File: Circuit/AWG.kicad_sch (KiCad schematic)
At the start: 28 parts, among them J1 Power, J2 Pump 1, J3 Pump 2, J4 Pump 3, M1 Fan_3pin, M2 Fan_3pin, Q1 RFP30N06LE, Q2 RFP30N06LE, SW1 Switch, U2 LCD-016N002L

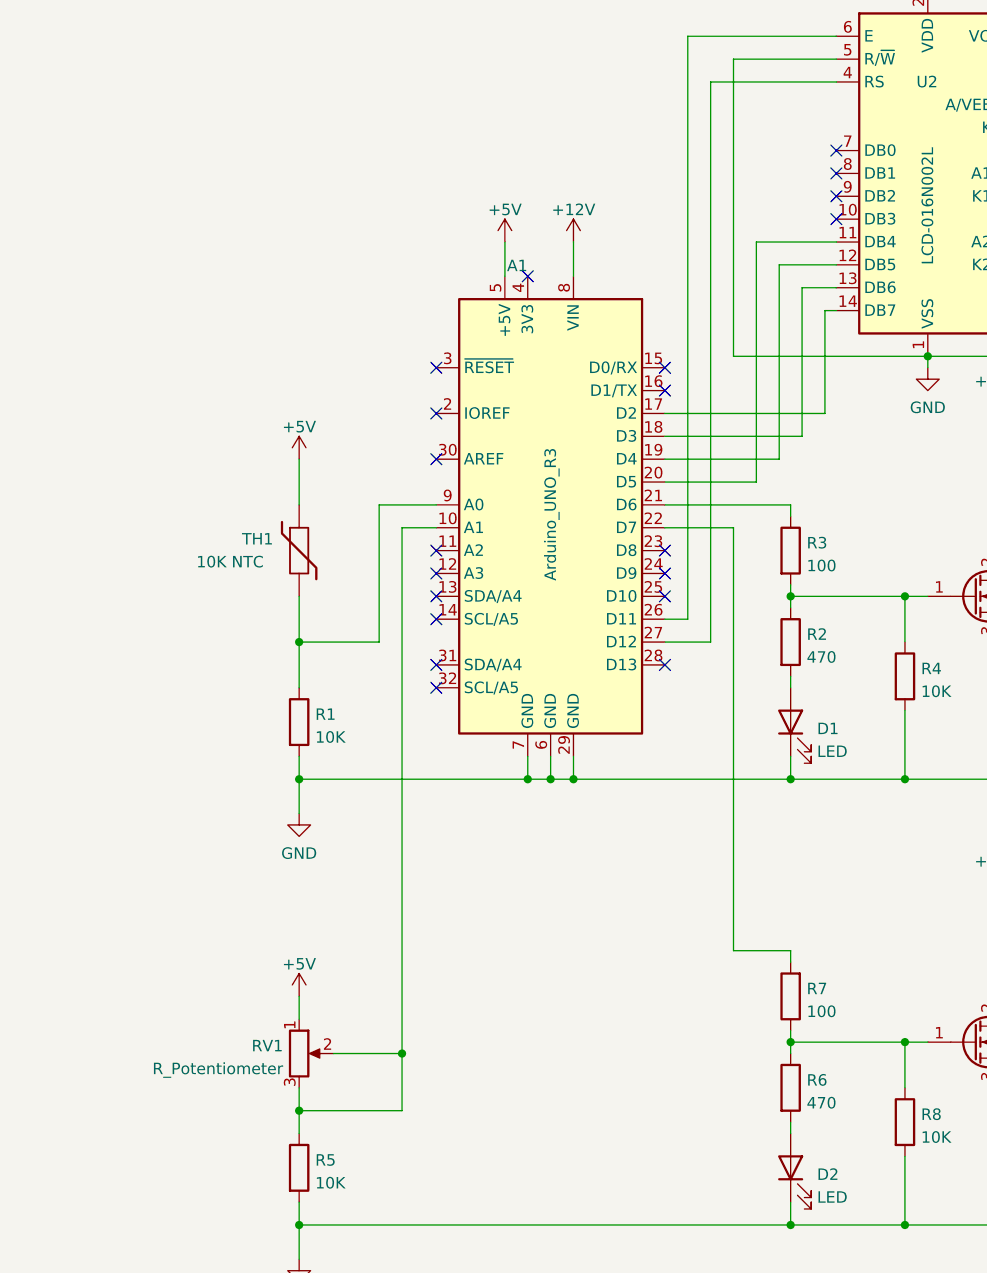
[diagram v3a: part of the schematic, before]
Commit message: [Circuit] Connect sensors to a digital output pin of the Arduino
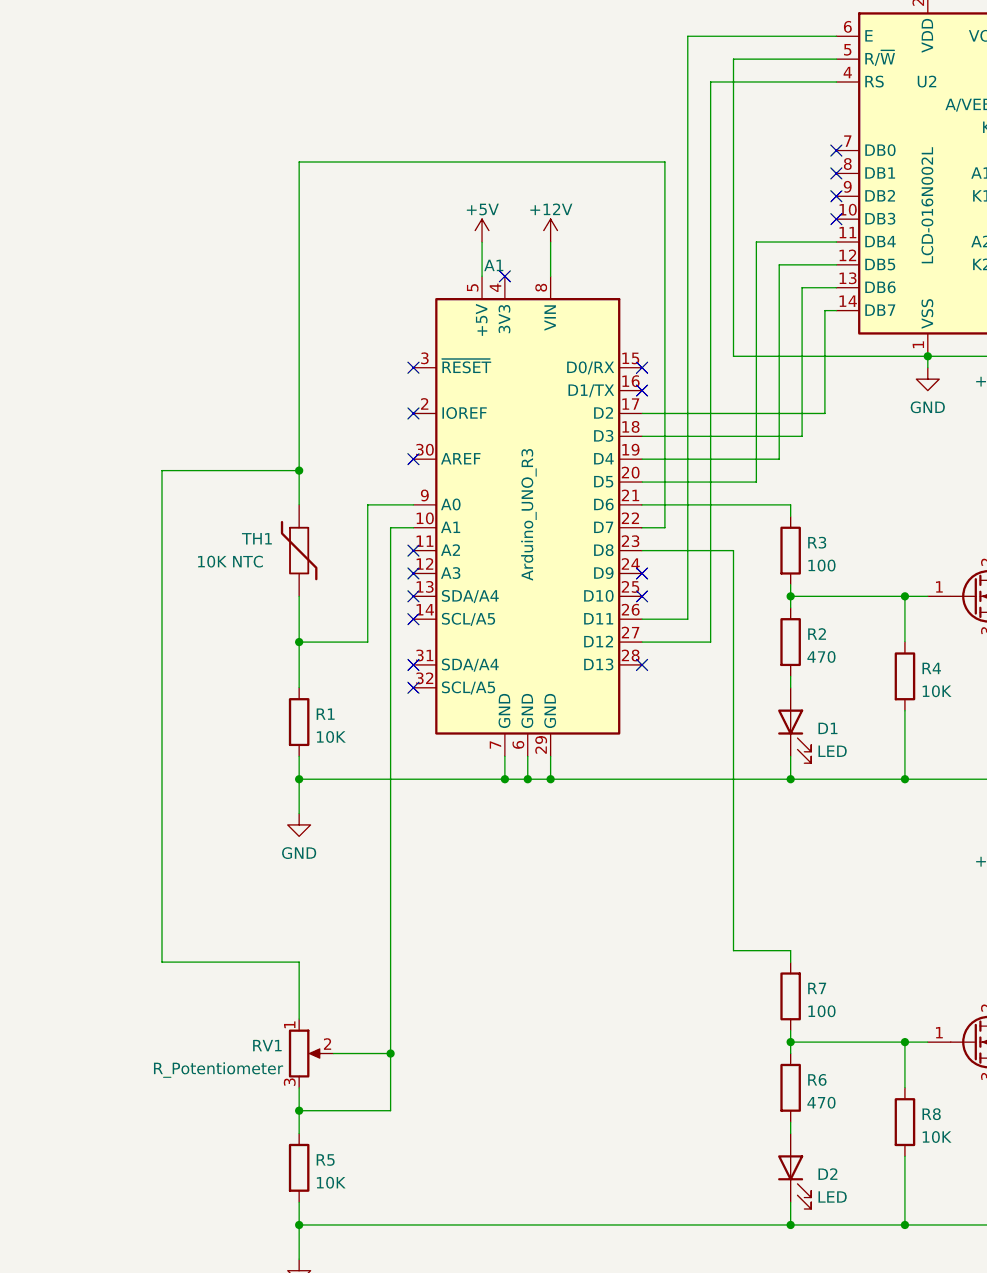
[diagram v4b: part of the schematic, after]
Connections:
- net +5V: no longer RV1.1, TH1.1
- net at A1.22 (D7): now also RV1.1, TH1.1; no longer R7.2
- net at A1.23 (D8): now also R7.2
- no-connect marks 26 -> 25
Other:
- moved on the sheet: A1

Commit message: [Circuit] Fix the NTC symbol
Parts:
- removed TH1: 10K NTC, Connector_PinHeader_2.54mm:PinHeader_1x02_P2.54mm_Vertical, symbol Device:Thermistor
- added TH1: 10K, Connector_PinHeader_2.54mm:PinHeader_1x02_P2.54mm_Vertical, symbol Device:Thermistor_NTC
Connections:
- net at A1.22 (D7), RV1.1: now also TH1.1
- net at A1.9 (A0), R1.1: now also TH1.2
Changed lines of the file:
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@@
     (stroke (width 0) (type default) (color 0 0 0 0))
   )
-  (wire (pts (xy 149.86 88.9) (xy 149.86 93.98))
+  (wire (pts (xy 149.86 87.63) (xy 149.86 93.98))
     (stroke (width 0) (type default) (color 0 0 0 0))
   )
@@
     (stroke (width 0) (type default) (color 0 0 0 0))
   )
-  (wire (pts (xy 149.86 74.93) (xy 149.86 78.74))
+  (wire (pts (xy 149.86 74.93) (xy 149.86 80.01))
     (stroke (width 0) (type default) (color 0 0 0 0))
   )
@@
     (pin "1")
   )
+  (symbol (lib_id "Device:Thermistor_NTC") (at 149.86 83.82 0) (unit 1)
+    (in_bom yes) (on_board yes) (fields_autoplaced)
+    (property "Reference" "TH1" (id 0) (at 152.273 83.3028 0)
+      (effects (font (size 1.27 1.27)) (justify left))
+    )
+    (property "Value" "10K" (id 1) (at 152.273 85.8397 0)
+      (effects (font (size 1.27 1.27)) (justify left))
+    )
+    (property "Footprint" "Connector_PinHeader_2.54mm:PinHeader_1x02_P2.54mm_Vertical" (id 2) (at 149.86 82.55 0)
+      (effects (font (size 1.27 1.27)) hide)
+    )
+    (property "Datasheet" "~" (id 3) (at 149.86 82.55 0)
+      (effects (font (size 1.27 1.27)) hide)
+    )
+    (pin "1")
+    (pin "2")
+  )
   (symbol (lib_id "Device:R") (at 204.47 143.51 0) (unit 1)
     (in_bom yes) (on_board yes) (fields_autoplaced)
@@
     )
     (pin "1")
-  )
-  (symbol (lib_id "Device:Thermistor") (at 149.86 83.82 0) (unit 1)
-    (in_bom yes) (on_board yes)
-    (property "Reference" "TH1" (id 0) (at 143.51 82.55 0)
-      (effects (font (size 1.27 1.27)) (justify left))
-    )
-    (property "Value" "10K NTC" (id 1) (at 138.43 85.09 0)
-      (effects (font (size 1.27 1.27)) (justify left))
-    )
-    (property "Footprint" "Connector_PinHeader_2.54mm:PinHeader_1x02_P2.54mm_Vertical" (id 2) (at 149.86 83.82 0)
-      (effects (font (size 1.27 1.27)) hide)
-    )
-    (property "Datasheet" "~" (id 3) (at 149.86 83.82 0)
-      (effects (font (size 1.27 1.27)) hide)
-    )
-    (pin "1")
-    (pin "2")
   )
   (symbol (lib_id "Device:R") (at 241.3 26.67 0) (unit 1)
@@
       (reference "SW1") (unit 1) (value "Switch") (footprint "Connector_PinHeader_2.54mm:PinHeader_1x03_P2.54mm_Vertical")
     )
-    (path "/a83da461-5696-4d85-8a08-2f5c13cd7d12"
-      (reference "TH1") (unit 1) (value "10K NTC") (footprint "Connector_PinHeader_2.54mm:PinHeader_1x02_P2.54mm_Vertical")
+    (path "/a129a5cd-9548-45aa-be27-45a3fe15e3e5"
+      (reference "TH1") (unit 1) (value "10K") (footprint "Connector_PinHeader_2.54mm:PinHeader_1x02_P2.54mm_Vertical")
     )
     (path "/e363f510-4f23-4a87-872a-5dd676ea4f99"

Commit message: [Circuit] Remove the unnecessary heatsinks
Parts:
- removed HS1, HS2: Heatsink, AWG:Heatsink_TO220_15x10mm, symbol Mechanical:Heatsink
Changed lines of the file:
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@@
     (pin "2")
-  )
-  (symbol (lib_id "Mechanical:Heatsink") (at 236.22 147.32 0) (unit 1)
-    (in_bom yes) (on_board yes) (fields_autoplaced)
-    (property "Reference" "HS2" (id 0) (at 239.8268 144.5803 0)
-      (effects (font (size 1.27 1.27)) (justify left))
-    )
-    (property "Value" "Heatsink" (id 1) (at 239.8268 147.1172 0)
-      (effects (font (size 1.27 1.27)) (justify left))
-    )
-    (property "Footprint" "AWG:Heatsink_TO220_15x10mm" (id 2) (at 236.5248 147.32 0)
-      (effects (font (size 1.27 1.27)) hide)
-    )
-    (property "Datasheet" "~" (id 3) (at 236.5248 147.32 0)
-      (effects (font (size 1.27 1.27)) hide)
-    )
   )
   (symbol (lib_id "power:+12V") (at 177.8 49.53 0) (unit 1)
@@
     (pin "3")
     (pin "4")
-  )
-  (symbol (lib_id "Mechanical:Heatsink") (at 236.22 96.52 0) (unit 1)
-    (in_bom yes) (on_board yes) (fields_autoplaced)
-    (property "Reference" "HS1" (id 0) (at 239.8268 93.7803 0)
-      (effects (font (size 1.27 1.27)) (justify left))
-    )
-    (property "Value" "Heatsink" (id 1) (at 239.8268 96.3172 0)
-      (effects (font (size 1.27 1.27)) (justify left))
-    )
-    (property "Footprint" "AWG:Heatsink_TO220_15x10mm" (id 2) (at 236.5248 96.52 0)
-      (effects (font (size 1.27 1.27)) hide)
-    )
-    (property "Datasheet" "~" (id 3) (at 236.5248 96.52 0)
-      (effects (font (size 1.27 1.27)) hide)
-    )
   )
   (symbol (lib_id "power:+5V") (at 170.18 49.53 0) (unit 1)
@@
       (reference "D2") (unit 1) (value "LED") (footprint "LED_THT:LED_D3.0mm_FlatTop")
     )
-    (path "/915d2328-ebfb-4215-86e4-fa27d5a9fb86"
-      (reference "HS1") (unit 1) (value "Heatsink") (footprint "AWG:Heatsink_TO220_15x10mm")
-    )
-    (path "/4f34fa7e-0493-4d5c-8308-e624f856cd7e"
-      (reference "HS2") (unit 1) (value "Heatsink") (footprint "AWG:Heatsink_TO220_15x10mm")
-    )
     (path "/7855fe26-79d5-4b43-a13f-918ed4b35748"

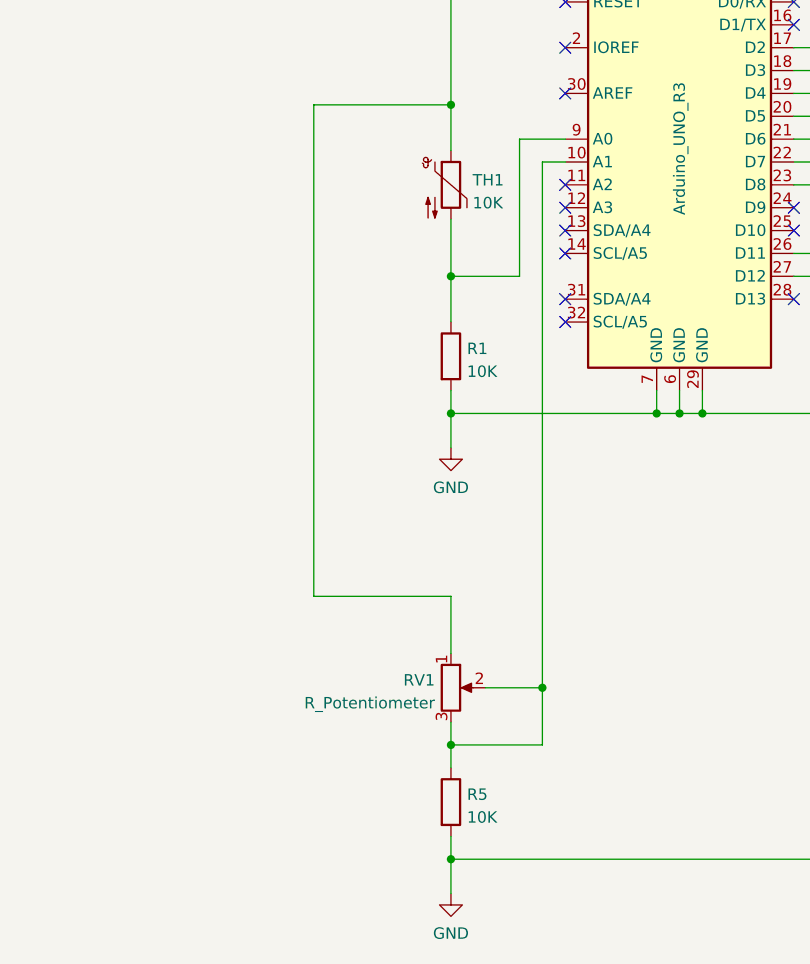
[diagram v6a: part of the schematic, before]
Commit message: [Circuit] Simplify the water level sensor to a connector
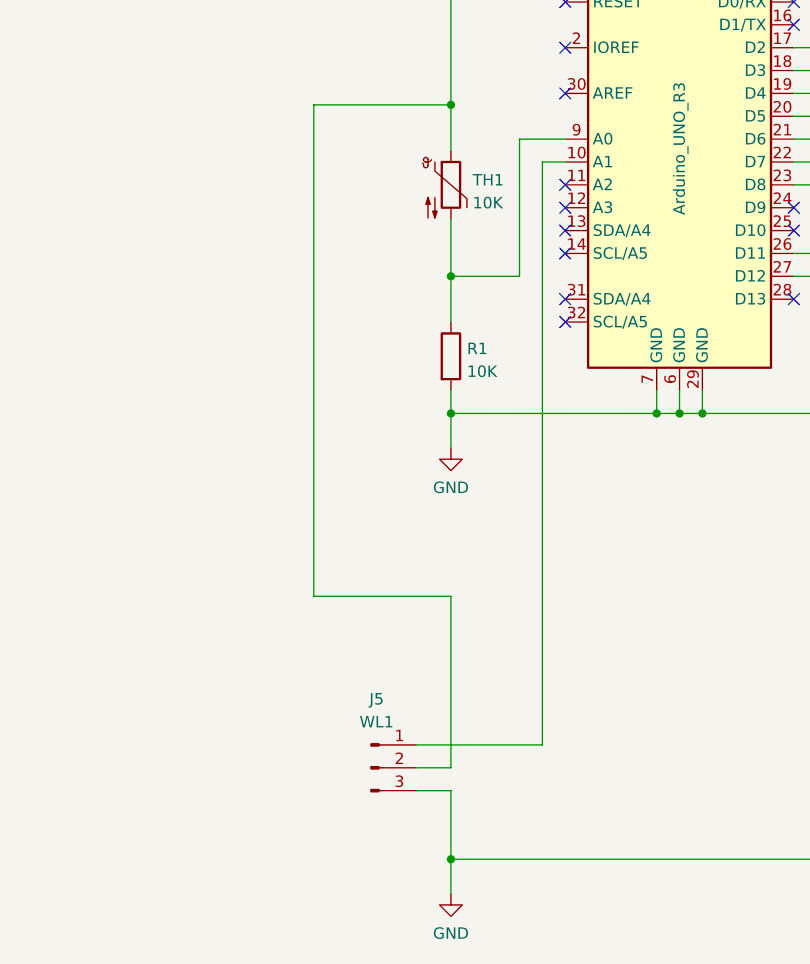
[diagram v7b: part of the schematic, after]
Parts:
- removed R5: 10K, Resistor_THT:R_Axial_DIN0207_L6.3mm_D2.5mm_P7.62mm_Horizontal, symbol Device:R
- removed RV1: R_Potentiometer, symbol Device:R_Potentiometer
- added J5: WL1, symbol Connector:Conn_01x03_Male
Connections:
- net GND: now also J5.3 (Pin_3)
- net at A1.22 (D7), TH1.1: now also J5.2 (Pin_2)
- net at A1.10 (A1): now also J5.1 (Pin_1)
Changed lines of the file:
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@@
   (junction (at 175.26 109.22) (diameter 0) (color 0 0 0 0)
   )
-  (junction (at 149.86 146.05) (diameter 0) (color 0 0 0 0)
-  )
   (junction (at 204.47 109.22) (diameter 0) (color 0 0 0 0)
   )
@@
   )
   (junction (at 149.86 158.75) (diameter 0) (color 0 0 0 0)
-  )
-  (junction (at 160.02 139.7) (diameter 0) (color 0 0 0 0)
   )
   (junction (at 149.86 74.93) (diameter 0) (color 0 0 0 0)
@@
     (stroke (width 0) (type default) (color 0 0 0 0))
   )
-  (wire (pts (xy 149.86 146.05) (xy 160.02 146.05))
-    (stroke (width 0) (type default) (color 0 0 0 0))
-  )
   (wire (pts (xy 39.37 148.59) (xy 39.37 151.13))
     (stroke (width 0) (type default) (color 0 0 0 0))
@@
     (stroke (width 0) (type default) (color 0 0 0 0))
   )
-  (wire (pts (xy 149.86 129.54) (xy 149.86 135.89))
+  (wire (pts (xy 149.86 129.54) (xy 149.86 148.59))
     (stroke (width 0) (type default) (color 0 0 0 0))
   )
@@
     (stroke (width 0) (type default) (color 0 0 0 0))
   )
-  (wire (pts (xy 149.86 146.05) (xy 149.86 148.59))
-    (stroke (width 0) (type default) (color 0 0 0 0))
-  )
   (wire (pts (xy 90.17 134.62) (xy 92.71 134.62))
     (stroke (width 0) (type default) (color 0 0 0 0))
@@
     (stroke (width 0) (type default) (color 0 0 0 0))
   )
-  (wire (pts (xy 149.86 156.21) (xy 149.86 158.75))
+  (wire (pts (xy 146.05 146.05) (xy 160.02 146.05))
+    (stroke (width 0) (type default) (color 0 0 0 0))
+  )
+  (wire (pts (xy 149.86 151.13) (xy 149.86 158.75))
     (stroke (width 0) (type default) (color 0 0 0 0))
   )
@@
     (stroke (width 0) (type default) (color 0 0 0 0))
   )
-  (wire (pts (xy 149.86 143.51) (xy 149.86 146.05))
-    (stroke (width 0) (type default) (color 0 0 0 0))
-  )
   (wire (pts (xy 49.53 72.39) (xy 49.53 74.93))
     (stroke (width 0) (type default) (color 0 0 0 0))
   )
-  (wire (pts (xy 160.02 139.7) (xy 160.02 146.05))
-    (stroke (width 0) (type default) (color 0 0 0 0))
-  )
   (wire (pts (xy 49.53 54.61) (xy 49.53 62.23))
     (stroke (width 0) (type default) (color 0 0 0 0))
@@
     (stroke (width 0) (type default) (color 0 0 0 0))
   )
-  (wire (pts (xy 160.02 81.28) (xy 160.02 139.7))
-    (stroke (width 0) (type default) (color 0 0 0 0))
-  )
-  (wire (pts (xy 153.67 139.7) (xy 160.02 139.7))
+  (wire (pts (xy 160.02 81.28) (xy 160.02 146.05))
+    (stroke (width 0) (type default) (color 0 0 0 0))
+  )
+  (wire (pts (xy 149.86 148.59) (xy 146.05 148.59))
     (stroke (width 0) (type default) (color 0 0 0 0))
   )
@@
   )
   (wire (pts (xy 57.15 57.15) (xy 54.61 57.15))
+    (stroke (width 0) (type default) (color 0 0 0 0))
+  )
+  (wire (pts (xy 146.05 151.13) (xy 149.86 151.13))
     (stroke (width 0) (type default) (color 0 0 0 0))
   )
@@
     )
     (pin "1")
-  )
-  (symbol (lib_id "Device:R_Potentiometer") (at 149.86 139.7 0) (unit 1)
-    (in_bom yes) (on_board yes) (fields_autoplaced)
-    (property "Reference" "RV1" (id 0) (at 148.0821 138.8653 0)
-      (effects (font (size 1.27 1.27)) (justify right))
-    )
-    (property "Value" "R_Potentiometer" (id 1) (at 148.0821 141.4022 0)
-      (effects (font (size 1.27 1.27)) (justify right))
-    )
-    (property "Footprint" "" (id 2) (at 149.86 139.7 0)
-      (effects (font (size 1.27 1.27)) hide)
-    )
-    (property "Datasheet" "~" (id 3) (at 149.86 139.7 0)
-      (effects (font (size 1.27 1.27)) hide)
-    )
-    (pin "1")
-    (pin "2")
-    (pin "3")
   )
   (symbol (lib_id "Connector:Conn_01x02_Male") (at 97.79 134.62 0) (mirror y) (unit 1)
@@
     (pin "2")
   )
+  (symbol (lib_id "Connector:Conn_01x03_Male") (at 140.97 148.59 0) (unit 1)
+    (in_bom yes) (on_board yes) (fields_autoplaced)
+    (property "Reference" "J5" (id 0) (at 141.605 140.97 0))
+    (property "Value" "WL1" (id 1) (at 141.605 143.51 0))
+    (property "Footprint" "" (id 2) (at 140.97 148.59 0)
+      (effects (font (size 1.27 1.27)) hide)
+    )
+    (property "Datasheet" "~" (id 3) (at 140.97 148.59 0)
+      (effects (font (size 1.27 1.27)) hide)
+    )
+    (pin "1")
+    (pin "2")
+    (pin "3")
+  )
   (symbol (lib_id "Device:LED") (at 204.47 102.87 90) (unit 1)
     (in_bom yes) (on_board yes) (fields_autoplaced)
@@
     (pin "2")
   )
-  (symbol (lib_id "Device:R") (at 149.86 152.4 0) (unit 1)
-    (in_bom yes) (on_board yes) (fields_autoplaced)
-    (property "Reference" "R5" (id 0) (at 151.638 151.5653 0)
-      (effects (font (size 1.27 1.27)) (justify left))
-    )
-    (property "Value" "10K" (id 1) (at 151.638 154.1022 0)
-      (effects (font (size 1.27 1.27)) (justify left))
-    )
-    (property "Footprint" "Resistor_THT:R_Axial_DIN0207_L6.3mm_D2.5mm_P7.62mm_Horizontal" (id 2) (at 148.082 152.4 90)
-      (effects (font (size 1.27 1.27)) hide)
-    )
-    (property "Datasheet" "~" (id 3) (at 149.86 152.4 0)
-      (effects (font (size 1.27 1.27)) hide)
-    )
-    (pin "1")
-    (pin "2")
-  )
   (symbol (lib_id "power:GND") (at 39.37 151.13 0) (mirror y) (unit 1)
     (in_bom yes) (on_board yes) (fields_autoplaced)
@@
       (reference "J4") (unit 1) (value "Pump 3") (footprint "Connector_PinHeader_2.54mm:PinHeader_1x02_P2.54mm_Vertical")
     )
+    (path "/ae472c6a-68b0-40da-ad06-e3c270d33133"
+      (reference "J5") (unit 1) (value "WL1") (footprint "")
+    )
     (path "/c6d538bd-1206-40d1-b447-a7e534cdd7eb"
       (reference "M1") (unit 1) (value "Fan_3pin") (footprint "Connector_PinHeader_2.54mm:PinHeader_1x03_P2.54mm_Vertical")
@@
       (reference "R4") (unit 1) (value "10K") (footprint "Resistor_THT:R_Axial_DIN0207_L6.3mm_D2.5mm_P7.62mm_Horizontal")
     )
-    (path "/f8c1b236-9562-4818-8114-2500039c74b5"
-      (reference "R5") (unit 1) (value "10K") (footprint "Resistor_THT:R_Axial_DIN0207_L6.3mm_D2.5mm_P7.62mm_Horizontal")
-    )
     (path "/a21b5a48-edbe-4741-bebb-18406636b412"
       (reference "R6") (unit 1) (value "470") (footprint "Resistor_THT:R_Axial_DIN0207_L6.3mm_D2.5mm_P7.62mm_Horizontal")
@@
       (reference "R9") (unit 1) (value "220") (footprint "Resistor_THT:R_Axial_DIN0207_L6.3mm_D2.5mm_P7.62mm_Horizontal")
     )
-    (path "/275f786d-13d5-472d-a3c7-d787b7b3830d"
-      (reference "RV1") (unit 1) (value "R_Potentiometer") (footprint "")
-    )
     (path "/df5d54c1-7bfe-4db0-97be-f9a59312f765"
